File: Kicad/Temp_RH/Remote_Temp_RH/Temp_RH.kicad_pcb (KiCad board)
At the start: 2 copper layers, 13 parts, among them J1 DHT 11, J2 Arduino, J3 DHT 22, J4 SHT 75, J5 SHT 31

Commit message: Kicad Current project update Kicad TH project update
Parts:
- removed C1: 1u, Capacitors_THT:CP_Radial_D4.0mm_P1.50mm
- removed D1, D2: LED, LEDs:LED_D1.8mm_W3.3mm_H2.4mm
- removed R5: 1k, Resistors_THT:R_Axial_DIN0204_L3.6mm_D1.6mm_P7.62mm_Horizontal
- added C2: 1u, Capacitors_THT:CP_Radial_D4.0mm_P1.50mm, F.Cu at (87.6, 118.1)
- added Decouplador1: 1u, Capacitors_THT:CP_Radial_D4.0mm_P1.50mm, F.Cu at (78.7, 118.1)
- added J7: NTC, Pin_Headers:Pin_Header_Straight_1x02_Pitch1.27mm, F.Cu at (90.2, 110.5)
- added J8: MLX, Pin_Headers:Pin_Header_Straight_1x04_Pitch1.27mm, F.Cu at (83.8, 110.5)
- J2: value Arduino -> DHT 22; footprint Connectors_Terminal_Blocks:TerminalBlock_Pheonix_MPT-2.54mm_10pol -> Pin_Headers:Pin_Header_Straight_1x04_Pitch1.27mm
- J3: value DHT 22 -> SHT 75
- J4: value SHT 75 -> Screw_Terminal_1x12; footprint Pin_Headers:Pin_Header_Straight_1x04_Pitch1.27mm -> Connectors_Terminal_Blocks:TerminalBlock_Pheonix_MPT-2.54mm_12pol
- R1, R2, R3: footprint Resistors_THT:R_Axial_DIN0204_L3.6mm_D1.6mm_P7.62mm_Horizontal -> Resistors_THT:R_Axial_DIN0204_L3.6mm_D1.6mm_P5.08mm_Horizontal
- R4: value 1k -> 10k; footprint Resistors_THT:R_Axial_DIN0204_L3.6mm_D1.6mm_P7.62mm_Horizontal -> Resistors_THT:R_Axial_DIN0204_L3.6mm_D1.6mm_P5.08mm_Horizontal
- moved J4 108.8 mm to (59.7, 125.7), turned to 0 degrees
- moved J3 106.8 mm to (67.3, 110.5)
- moved J1 99.4 mm to (52.1, 110.5)
- moved R4 96.5 mm to (67.3, 119.4), turned to 0 degrees
- moved R1 94.4 mm to (59.7, 119.4), turned to 180 degrees
- moved J5 93.2 mm to (73.7, 110.5)
- moved R2 93.2 mm to (59.7, 116.8), turned to 180 degrees
- moved R3 86.7 mm to (72.4, 116.8), turned to 180 degrees
- moved J2 81.8 mm to (59.7, 110.5), turned to 90 degrees
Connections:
- J1 pad 2: /Data_DHT11 -> Net-(J1-Pad2)
- J1 pad 3: (no net) -> Net-(J1-Pad3)
- J2 pad 1: /Data_DHT11 -> +3V3
- J2 pad 2: Net-(J2-Pad2) -> /Clock75
- J2 pad 3: /DataSHT75 -> Net-(J2-Pad3)
- J2 pad 4: +3V3 -> GND
- J3 pad 1: +3V3 -> Net-(J3-Pad1)
- J3 pad 2: Net-(J2-Pad2) -> +3V3
- J3 pad 4: (no net) -> Net-(J3-Pad4)
- J4 pad 1: Net-(J2-Pad6) -> GND
- J4 pad 3: GND -> Net-(J1-Pad2)
- J4 pad 4: /DataSHT75 -> /Clock75
- J5 pad 1: (no net) -> Net-(J5-Pad1)
- J5 pad 3: (no net) -> Net-(J5-Pad3)
- J5 pad 4: /SDA -> /SCL31
- J5 pad 5: /SCL -> Net-(J4-Pad8)
- R1 pad 1: +3V3 -> Net-(J1-Pad2)
- R1 pad 2: /Data_DHT11 -> +3V3
- R2 pad 1: +3V3 -> /Clock75
- R2 pad 2: Net-(J2-Pad2) -> +3V3
- R3 pad 1: +3V3 -> Net-(J3-Pad4)
- R3 pad 2: /DataSHT75 -> +3V3
- R4 pad 1: /LedOut -> Net-(J4-Pad9)
- R4 pad 2: Net-(D1-Pad2) -> GND
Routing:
- net Net-(J2-Pad2): track 48.6 -> 0.00 mm, vias 4 -> 0
- net Net-(J4-Pad9): track 0.00 -> 41.9 mm, vias 0 -> 4
- net Net-(J4-Pad11): track 0.00 -> 30.5 mm, vias 0 -> 4
- net Net-(J4-Pad10): track 0.00 -> 29.2 mm, vias 0 -> 6
- net /Data_DHT11: track 29.2 -> 0.00 mm, vias 2 -> 0
- net /DataSHT75: track 29.2 -> 0.00 mm, vias 6 -> 0
- net Net-(J1-Pad2): track 0.00 -> 29.2 mm
- net Net-(J2-Pad6): track 27.0 -> 0.00 mm, vias 4 -> 0
- net /SDA: track 25.4 -> 0.00 mm, vias 2 -> 0
- net /SCL: track 24.1 -> 0.00 mm, vias 2 -> 0
- net Net-(J4-Pad8): track 0.00 -> 24.1 mm, vias 0 -> 6
- net /Clock75: track 0.00 -> 22.9 mm
- net Net-(J3-Pad1): track 0.00 -> 20.3 mm, vias 0 -> 2
- net Net-(J3-Pad4): track 0.00 -> 19.0 mm, vias 0 -> 4
- net /SCL31: track 0.00 -> 17.8 mm, vias 0 -> 4
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
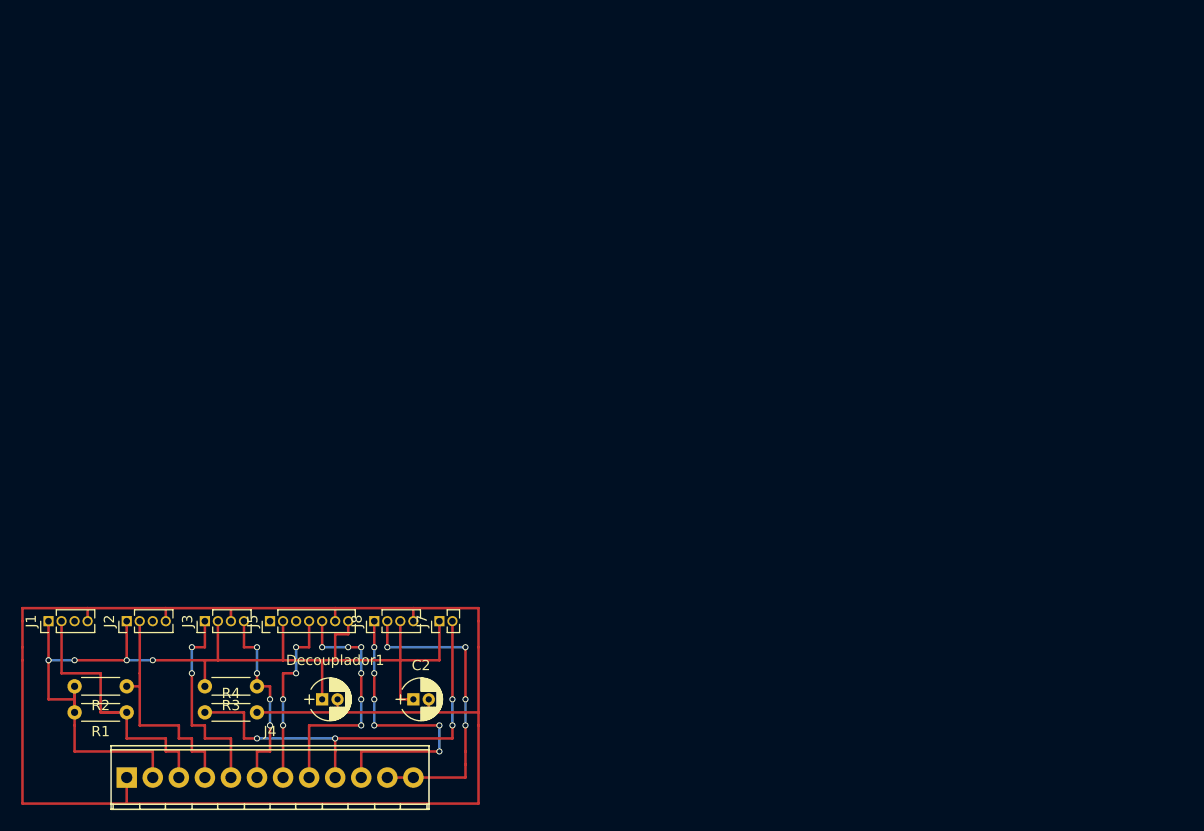
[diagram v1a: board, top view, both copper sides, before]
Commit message: Revision V2.0! New version of remote aquisition system for Temperature and humidity.
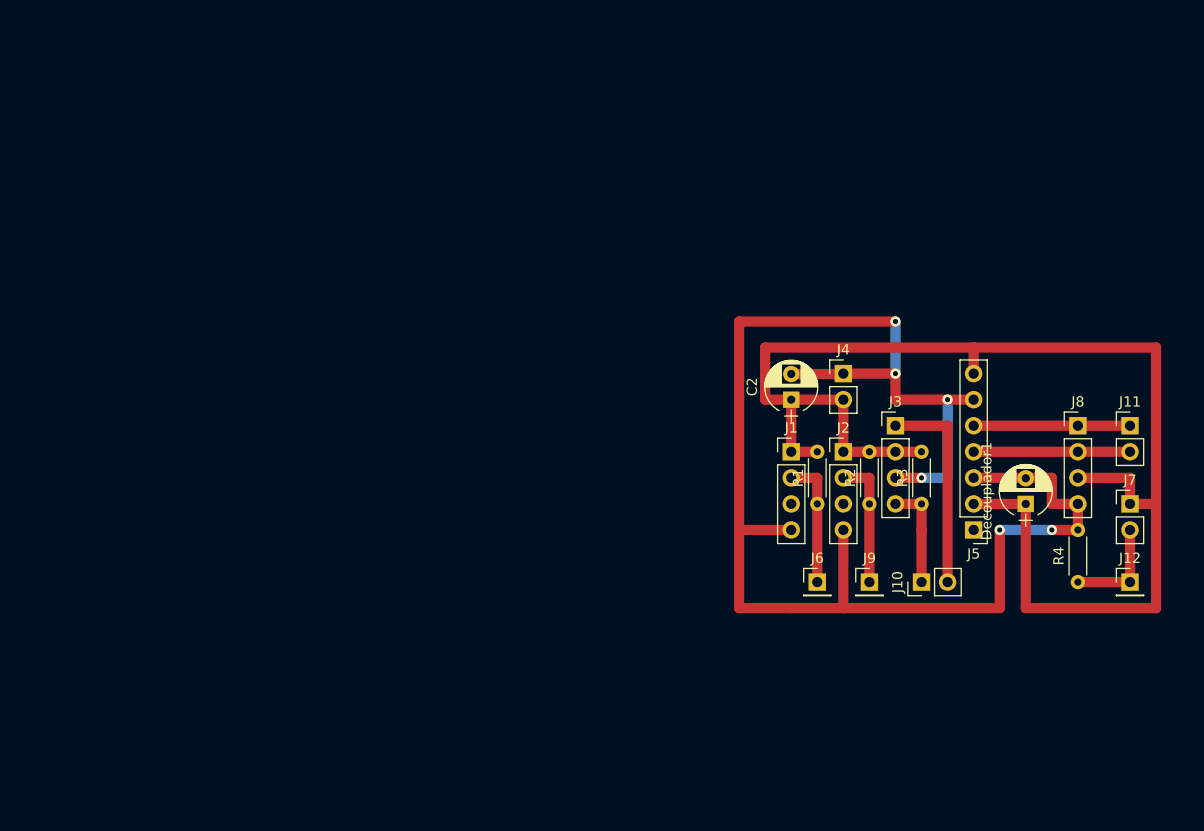
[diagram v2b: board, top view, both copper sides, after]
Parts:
- added J10: CONN_01X02, Pin_Headers:Pin_Header_Straight_1x02_Pitch2.54mm, F.Cu at (137.2, 106.7)
- added J11: CONN_01X02, Pin_Headers:Pin_Header_Straight_1x02_Pitch2.54mm, F.Cu at (157.5, 91.4)
- added J12: CONN_01X01, Pin_Headers:Pin_Header_Straight_1x01_Pitch2.54mm, F.Cu at (157.5, 106.7)
- added J6: CONN_01X01, Pin_Headers:Pin_Header_Straight_1x01_Pitch2.54mm, F.Cu at (127.0, 106.7)
- added J9: CONN_01X01, Pin_Headers:Pin_Header_Straight_1x01_Pitch2.54mm, F.Cu at (132.1, 106.7)
- C2, Decouplador1: footprint Capacitors_THT:CP_Radial_D4.0mm_P1.50mm -> Capacitors_THT:CP_Radial_D5.0mm_P2.50mm
- J1, J2, J3, J8: footprint Pin_Headers:Pin_Header_Straight_1x04_Pitch1.27mm -> Pin_Headers:Pin_Header_Straight_1x04_Pitch2.54mm
- J4: value Screw_Terminal_1x12 -> CONN_01X02; footprint Connectors_Terminal_Blocks:TerminalBlock_Pheonix_MPT-2.54mm_12pol -> Pin_Headers:Pin_Header_Straight_1x02_Pitch2.54mm
- J5: footprint Pin_Headers:Pin_Header_Straight_1x07_Pitch1.27mm -> Pin_Headers:Pin_Header_Straight_1x07_Pitch2.54mm
- J7: footprint Pin_Headers:Pin_Header_Straight_1x02_Pitch1.27mm -> Pin_Headers:Pin_Header_Straight_1x02_Pitch2.54mm
- moved R4 86.0 mm to (152.4, 106.7), turned to 90 degrees
- moved J4 80.2 mm to (129.5, 86.4)
- moved R2 74.5 mm to (132.1, 99.1), turned to 90 degrees
- moved J1 74.2 mm to (124.5, 94.0), turned to 0 degrees
- moved J2 71.8 mm to (129.5, 94.0), turned to 0 degrees
- moved J8 71.2 mm to (152.4, 91.4), turned to 0 degrees
- moved Decouplador1 71.2 mm to (147.3, 99.1), turned to 90 degrees
- moved R1 70.3 mm to (127.0, 99.1), turned to 90 degrees
- moved J3 70.0 mm to (134.6, 91.4), turned to 0 degrees
- moved J5 69.2 mm to (142.2, 101.6), turned to 180 degrees
- moved J7 68.3 mm to (157.5, 99.1), turned to 0 degrees
- moved R3 67.2 mm to (137.2, 99.1), turned to 90 degrees
- moved C2 47.0 mm to (124.5, 88.9), turned to 90 degrees
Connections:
- J1 pad 2: Net-(J1-Pad2) -> /Data11
- J2 pad 2: /Clock75 -> /Data22
- J3 pad 1: Net-(J3-Pad1) -> /Clock75
- J3 pad 4: Net-(J3-Pad4) -> /Data75
- J5 pad 3: Net-(J5-Pad3) -> GND
- J5 pad 4: /SCL31 -> /SDA
- J5 pad 5: Net-(J4-Pad8) -> /SCL
- J7 pad 2: Net-(J4-Pad9) -> /DataNTC
- J8 pad 1: Net-(J4-Pad10) -> /SCL
- J8 pad 2: Net-(J4-Pad11) -> /SDA
- R1 pad 1: Net-(J1-Pad2) -> /Data11
- R2 pad 1: /Clock75 -> /Data22
- R3 pad 1: Net-(J3-Pad4) -> /Data75
- R4 pad 1: Net-(J4-Pad9) -> /DataNTC
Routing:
- net Net-(J4-Pad9): track 41.9 -> 0.00 mm, vias 4 -> 0
- net +3V3: track 102.9 -> 137.2 mm, vias 4 -> 0
- net Net-(J4-Pad11): track 30.5 -> 0.00 mm, vias 4 -> 0
- net Net-(J4-Pad10): track 29.2 -> 0.00 mm, vias 6 -> 0
- net Net-(J1-Pad2): track 29.2 -> 0.00 mm
- net Net-(J4-Pad8): track 24.1 -> 0.00 mm, vias 6 -> 0
- net Net-(J3-Pad1): track 20.3 -> 0.00 mm, vias 2 -> 0
- net Net-(J3-Pad4): track 19.0 -> 0.00 mm, vias 4 -> 0
- net /SCL31: track 17.8 -> 0.00 mm, vias 4 -> 0
- net /SDA: track 0.00 -> 15.2 mm
- net /SCL: track 0.00 -> 15.2 mm
- net /Data22: track 0.00 -> 12.7 mm
- net /Data11: track 0.00 -> 12.7 mm
- net GND: track 160.7 -> 149.9 mm, vias 0 -> 6
- net /DataNTC: track 0.00 -> 10.2 mm
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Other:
- net class Default: clearance 0.2 -> 0.5; trace_width 0.25 -> 1; via_dia 0.6 -> 1; via_drill 0.4 -> 0.5
- rule trace_clearance: 0.2 -> 0.5
- rule trace_min: 0.2 -> 1
- rule via_min_size: 0.4 -> 0.5
